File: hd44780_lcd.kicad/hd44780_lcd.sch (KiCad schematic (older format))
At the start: 3 parts, among them U1 PIC12F675-IP, U2 74HC595

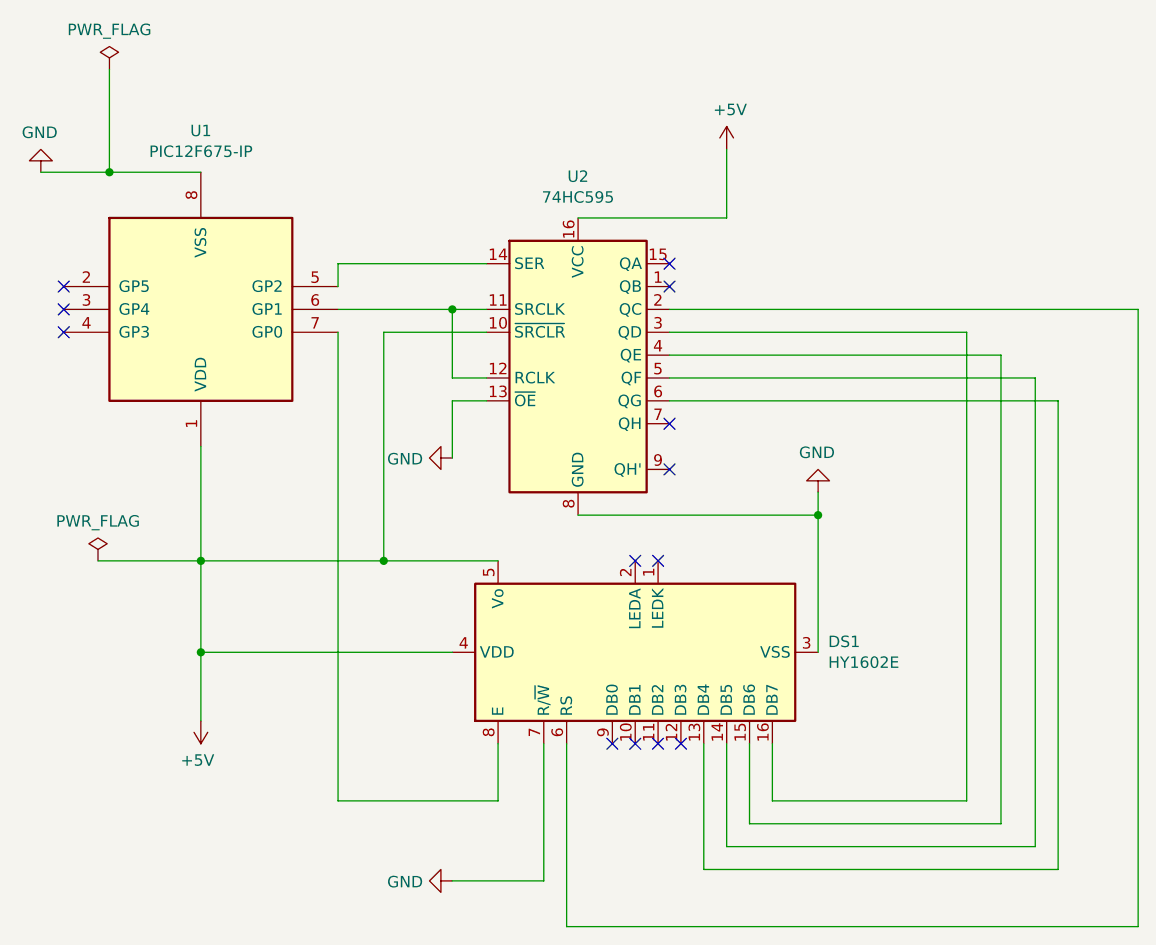
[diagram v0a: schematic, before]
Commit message: Rev 2: replaced LCD-component (to match pin-order)
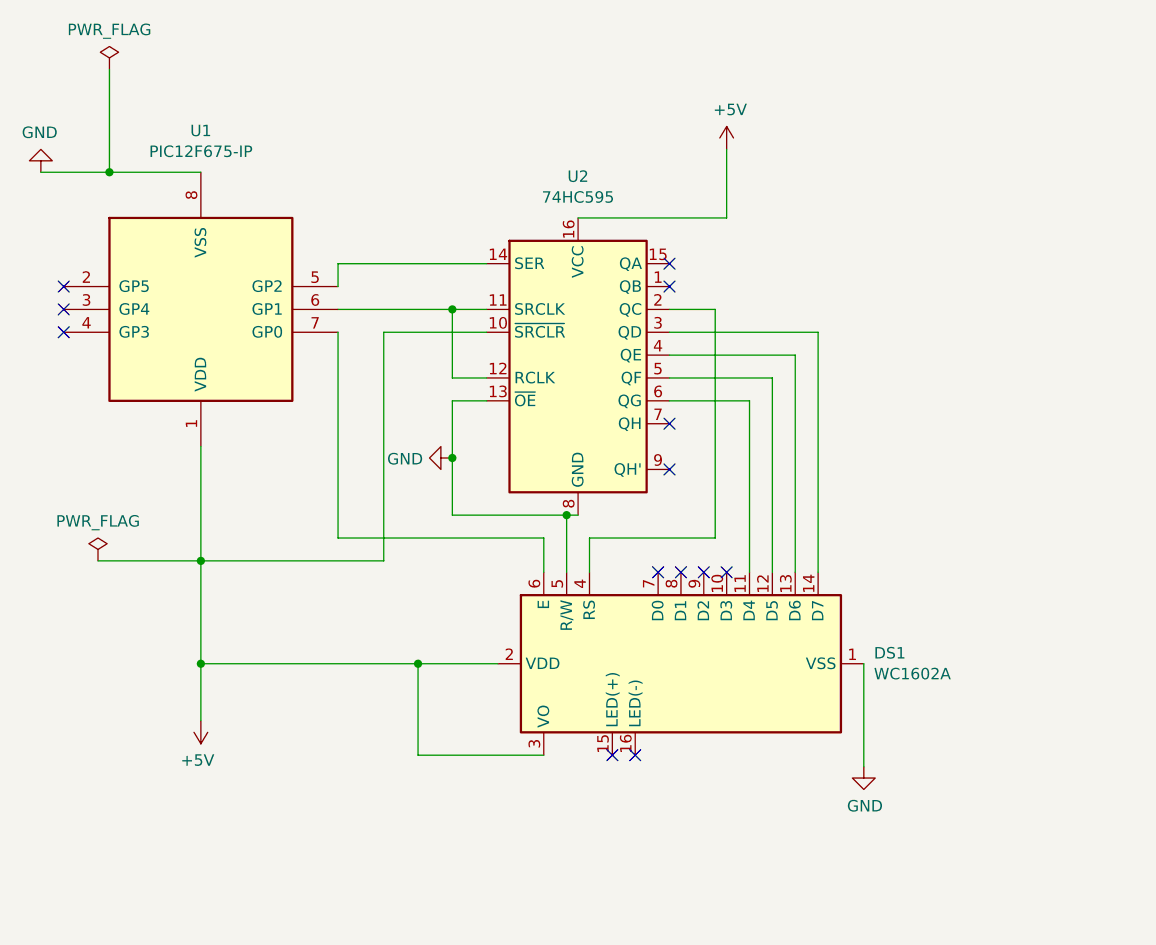
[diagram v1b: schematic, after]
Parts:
- removed DS1: HY1602E, Display:HY1602E, symbol Display_Character:HY1602E
- added DS1: WC1602A, Display:WC1602A, symbol Display_Character:WC1602A
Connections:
- net +5V: now also DS1.2 (VDD), DS1.3 (VO)
- net GND: now also DS1.1 (VSS), DS1.5 (R/W)
- net at U1.7 (GP0): now also DS1.6 (E)
- net at U2.2 (QC): now also DS1.4 (RS)
- net at U2.3 (QD): now also DS1.14 (D7)
- net at U2.4 (QE): now also DS1.13 (D6)
- net at U2.5 (QF): now also DS1.12 (D5)
- net at U2.6 (QG): now also DS1.11 (D4)
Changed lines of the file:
@@
 Sheet 1 1
 Title "PIC12F675 with HD44780 LCD"
-Date "2020-03-20"
-Rev "1"
+Date "2020-03-21"
+Rev "2"
 Comp "Bernhard Bablok"
 Comment1 "https://github.com/bablokb/pic-toolchain/src/hd44780_lcd"
@@
 $EndComp
 Wire Wire Line
-	3400 3050 3400 5100
-Wire Wire Line
-	3400 5100 4100 5100
-Wire Wire Line
-	4100 5100 4100 4850
-Wire Wire Line
 	3400 2950 3900 2950
 Wire Wire Line
@@
 Wire Wire Line
 	3400 2750 4050 2750
-Wire Wire Line
-	4850 3350 6550 3350
-Wire Wire Line
-	6550 3350 6550 5400
-Wire Wire Line
-	6550 5400 5000 5400
-Wire Wire Line
-	5000 5400 5000 4850
-Wire Wire Line
-	4850 3250 6450 3250
-Wire Wire Line
-	6450 3250 6450 5300
-Wire Wire Line
-	6450 5300 5100 5300
-Wire Wire Line
-	5100 5300 5100 4850
-Wire Wire Line
-	4850 3150 6300 3150
-Wire Wire Line
-	6300 3150 6300 5200
-Wire Wire Line
-	6300 5200 5200 5200
-Wire Wire Line
-	5200 5200 5200 4850
-Wire Wire Line
-	4850 3050 6150 3050
-Wire Wire Line
-	6150 5100 5300 5100
-Wire Wire Line
-	5300 5100 5300 4850
-Wire Wire Line
-	6150 3050 6150 5100
-Wire Wire Line
-	4850 2950 6900 2950
-Wire Wire Line
-	6900 2950 6900 5650
-Wire Wire Line
-	6900 5650 4400 5650
-Wire Wire Line
-	4400 5650 4400 4850
 Wire Wire Line
 	4050 3250 3900 3250
@@
 NoConn ~ 2200 2950
 NoConn ~ 2200 2850
-NoConn ~ 4700 4050
-NoConn ~ 4800 4050
-$Comp
-L power:+5V #PWR03
+$Comp
+L power:+5V #PWR02
 U 1 1 5E75C959
 P 2800 4750
-F 0 "#PWR03" H 2800 4600 50  0001 C CNN
+F 0 "#PWR02" H 2800 4600 50  0001 C CNN
 F 1 "+5V" H 2815 4923 50  0000 C CNN
 F 2 "" H 2800 4750 50  0001 C CNN
@@
 $EndComp
 Wire Wire Line
-	3900 4450 2800 4450
-Connection ~ 2800 4450
-Wire Wire Line
-	2800 4450 2800 4750
-Wire Wire Line
 	2800 3550 2800 4050
 Connection ~ 2800 4050
 $Comp
-L power:GND #PWR02
+L power:GND #PWR05
 U 1 1 5E75FCDB
-P 5500 3750
-F 0 "#PWR02" H 5500 3500 50  0001 C CNN
-F 1 "GND" H 5505 3577 50  0000 C CNN
-F 2 "" H 5500 3750 50  0001 C CNN
-F 3 "" H 5500 3750 50  0001 C CNN
-	1    5500 3750
-	-1   0    0    1
+P 5700 4950
+F 0 "#PWR05" H 5700 4700 50  0001 C CNN
+F 1 "GND" H 5705 4777 50  0000 C CNN
+F 2 "" H 5700 4950 50  0001 C CNN
+F 3 "" H 5700 4950 50  0001 C CNN
+	1    5700 4950
+	1    0    0    -1
 $EndComp
 $Comp
@@
 $EndComp
 $Comp
-L power:PWR_FLAG #FLG01
+L power:PWR_FLAG #FLG02
 U 1 1 5E762FBF
 P 2400 1900
-F 0 "#FLG01" H 2400 1975 50  0001 C CNN
+F 0 "#FLG02" H 2400 1975 50  0001 C CNN
 F 1 "PWR_FLAG" H 2400 2073 50  0000 C CNN
 F 2 "" H 2400 1900 50  0001 C CNN
@@
 $EndComp
 $Comp
-L power:PWR_FLAG #FLG02
+L power:PWR_FLAG #FLG01
 U 1 1 5E7638B3
 P 2350 4050
-F 0 "#FLG02" H 2350 4125 50  0001 C CNN
+F 0 "#FLG01" H 2350 4125 50  0001 C CNN
 F 1 "PWR_FLAG" H 2350 4223 50  0000 C CNN
 F 2 "" H 2350 4050 50  0001 C CNN
@@
 Wire Wire Line
 	2350 4050 2800 4050
-Wire Wire Line
-	2800 4050 2800 4450
 NoConn ~ 4850 2750
 NoConn ~ 4850 2850
-NoConn ~ 4600 4850
-NoConn ~ 4700 4850
-NoConn ~ 4800 4850
-NoConn ~ 4900 4850
-$Comp
-L power:GND #PWR0101
-U 1 1 5E769C07
-P 3900 5450
-F 0 "#PWR0101" H 3900 5200 50  0001 C CNN
-F 1 "GND" V 3905 5322 50  0000 R CNN
-F 2 "" H 3900 5450 50  0001 C CNN
-F 3 "" H 3900 5450 50  0001 C CNN
-	1    3900 5450
-	0    1    1    0
-$EndComp
-Wire Wire Line
-	4300 4850 4300 5450
-Wire Wire Line
-	4300 5450 3900 5450
-Wire Wire Line
-	4450 3850 5500 3850
-Wire Wire Line
-	5500 3750 5500 3850
-Connection ~ 5500 3850
-Wire Wire Line
-	5500 3850 5500 4450
-$Comp
-L power:+5V #PWR0102
+$Comp
+L power:+5V #PWR04
 U 1 1 5E76D739
 P 5100 2250
-F 0 "#PWR0102" H 5100 2100 50  0001 C CNN
+F 0 "#PWR04" H 5100 2100 50  0001 C CNN
 F 1 "+5V" H 5115 2423 50  0000 C CNN
 F 2 "" H 5100 2250 50  0001 C CNN
@@
 	2800 4050 3600 4050
 $Comp
-L power:GND #PWR0103
+L power:GND #PWR03
 U 1 1 5E7705B3
 P 3900 3600
-F 0 "#PWR0103" H 3900 3350 50  0001 C CNN
+F 0 "#PWR03" H 3900 3350 50  0001 C CNN
 F 1 "GND" V 3905 3472 50  0000 R CNN
 F 2 "" H 3900 3600 50  0001 C CNN
@@
 Wire Wire Line
 	3600 3050 3600 4050
-Connection ~ 3600 4050
-Wire Wire Line
-	3600 4050 4100 4050
-$Comp
-L Display_Character:HY1602E DS1
-U 1 1 5E75126E
-P 4700 4450
-F 0 "DS1" V 4746 3606 50  0000 R CNN
-F 1 "HY1602E" V 4655 3606 50  0000 R CNN
-F 2 "Display:HY1602E" H 4700 3550 50  0001 C CIN
-F 3 "http://www.icbank.com/data/ICBShop/board/HY1602E.pdf" H 4900 4550 50  0001 C CNN
-	1    4700 4450
-	0    -1   -1   0
-$EndComp
+$Comp
+L Display_Character:WC1602A DS1
+U 1 1 5E75E076
+P 4900 4500
+F 0 "DS1" V 4854 3656 50  0000 R CNN
+F 1 "WC1602A" V 4945 3656 50  0000 R CNN
+F 2 "Display:WC1602A" H 4900 3600 50  0001 C CIN
+F 3 "http://www.wincomlcd.com/pdf/WC1602A-SFYLYHTC06.pdf" H 5600 4500 50  0001 C CNN
+	1    4900 4500
+	0    -1   1    0
+$EndComp
+Wire Wire Line
+	2800 4050 2800 4500
+Wire Wire Line
+	5700 4950 5700 4500
+Wire Wire Line
+	4100 4500 3750 4500
+Connection ~ 2800 4500
+Wire Wire Line
+	2800 4500 2800 4750
+Wire Wire Line
+	4300 4900 3750 4900
+Wire Wire Line
+	3750 4900 3750 4500
+Connection ~ 3750 4500
+Wire Wire Line
+	3750 4500 2800 4500
+Wire Wire Line
+	3400 3050 3400 3950
+Wire Wire Line
+	3400 3950 4300 3950
+Wire Wire Line
+	4300 3950 4300 4100
+Wire Wire Line
+	4450 3850 4400 3850
+Wire Wire Line
+	3900 3850 3900 3600
+Connection ~ 3900 3600
+Wire Wire Line
+	4850 3350 5200 3350
+Wire Wire Line
+	5200 3350 5200 4100
+Wire Wire Line
+	4850 3250 5300 3250
+Wire Wire Line
+	5300 3250 5300 4100
+Wire Wire Line
+	4850 3150 5400 3150
+Wire Wire Line
+	5400 3150 5400 4100
+Wire Wire Line
+	4850 3050 5500 3050
+Wire Wire Line
+	5500 3050 5500 4100
+Wire Wire Line
+	4850 2950 5050 2950
+Wire Wire Line
+	5050 2950 5050 3950
+Wire Wire Line
+	5050 3950 4500 3950
+Wire Wire Line
+	4500 3950 4500 4100
+NoConn ~ 5100 4100
+NoConn ~ 5000 4100
+NoConn ~ 4900 4100
+NoConn ~ 4800 4100
+NoConn ~ 4700 4900
+NoConn ~ 4600 4900
+Wire Wire Line
+	4400 4100 4400 3850
+Connection ~ 4400 3850
+Wire Wire Line
+	4400 3850 3900 3850
 $EndSCHEMATC
